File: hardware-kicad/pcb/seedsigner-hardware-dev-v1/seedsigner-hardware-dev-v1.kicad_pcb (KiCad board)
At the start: 2 copper layers, 14 x 23 mm, 17 parts, among them U1 LuckFox_Pico_MINI, U2 WAVESHARE_LCD_BUTTON_BOARD_1.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

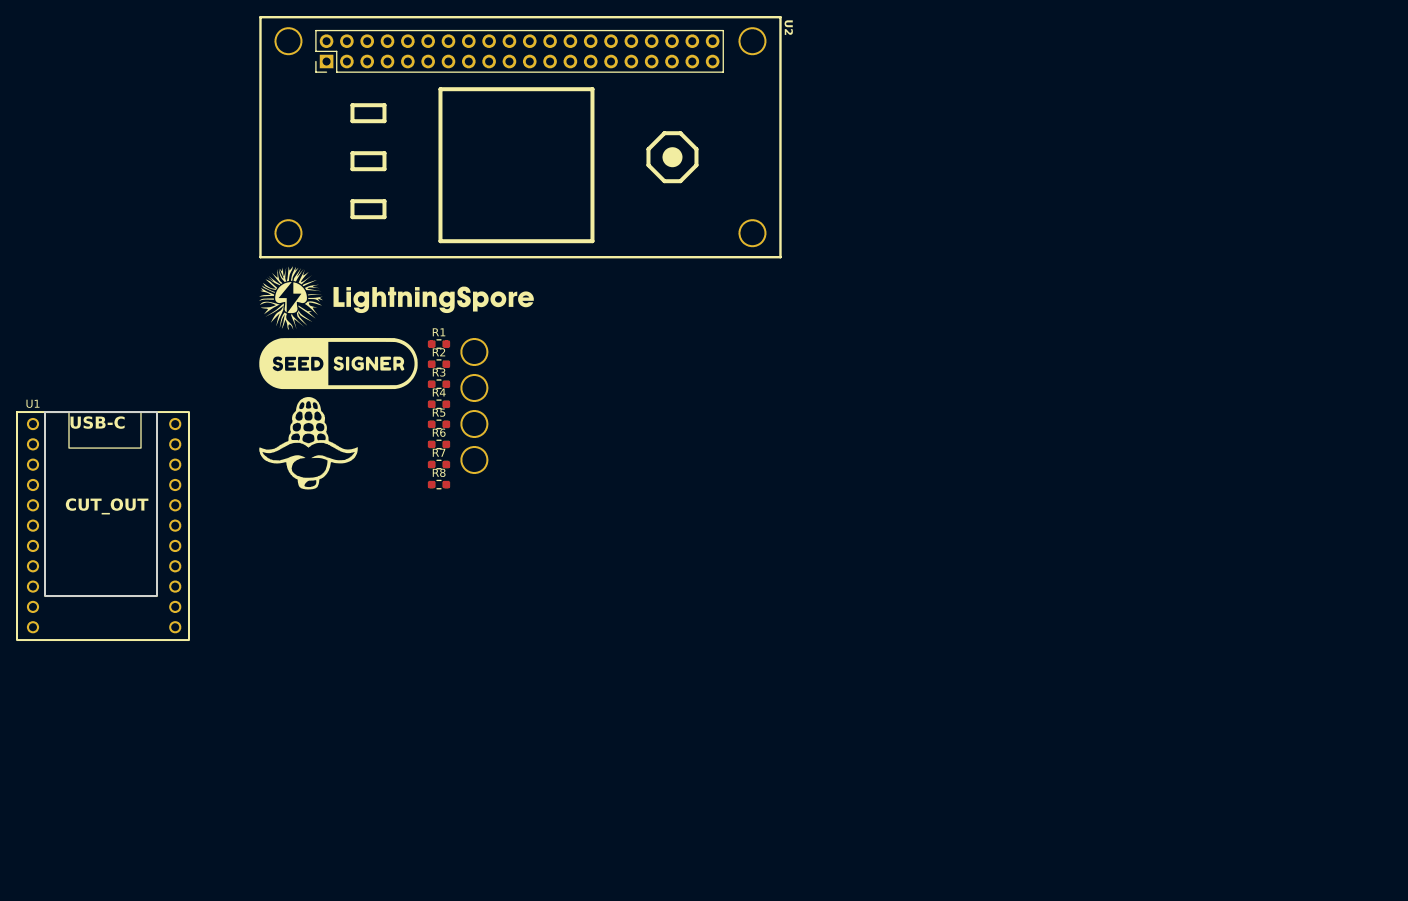
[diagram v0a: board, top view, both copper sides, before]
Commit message: seedsigner hardware dev v1 all footprints created and placed
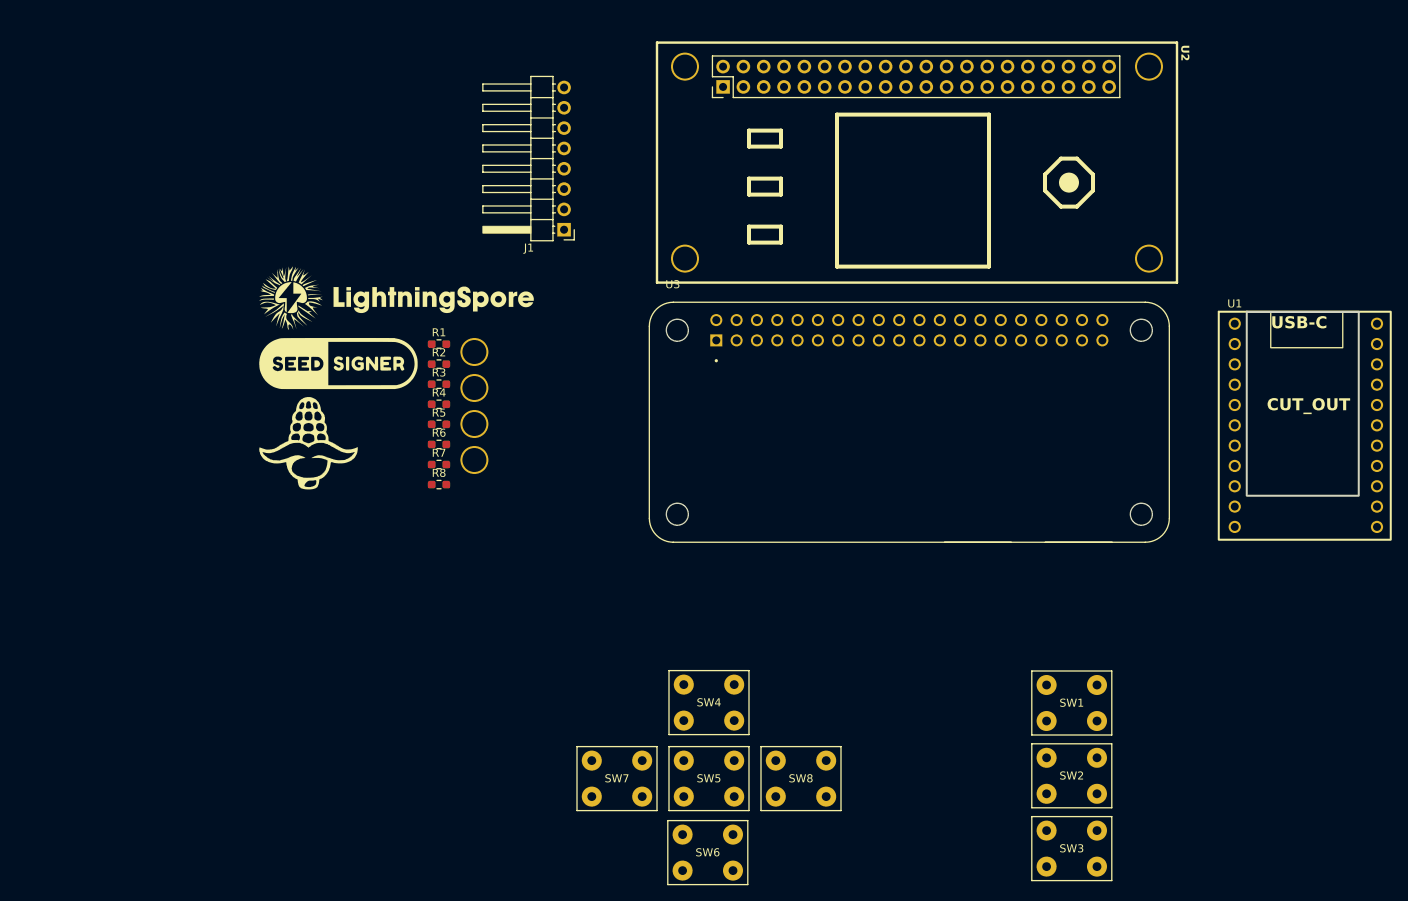
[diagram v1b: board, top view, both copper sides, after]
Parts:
- added J1: Conn_01x08_MountingPin, Connector_PinHeader_2.54mm:PinHeader_1x08_P2.54mm_Horizontal, F.Cu at (87.4, 74.9)
- added SW1: SW_Push, seedsigner-luckfox:BTN_SPST_NO_PTH, F.Cu at (150.8, 134.1)
- added SW2: SW_Push, seedsigner-luckfox:BTN_SPST_NO_PTH, F.Cu at (150.8, 143.2)
- added SW3: SW_Push, seedsigner-luckfox:BTN_SPST_NO_PTH, F.Cu at (150.8, 152.2)
- added SW4: SW_Push, seedsigner-luckfox:BTN_SPST_NO_PTH, F.Cu at (105.5, 134.0)
- added SW5: SW_Push, seedsigner-luckfox:BTN_SPST_NO_PTH, F.Cu at (105.5, 143.5)
- added SW6: SW_Push, seedsigner-luckfox:BTN_SPST_NO_PTH, F.Cu at (105.3, 152.8)
- added SW7: SW_Push, seedsigner-luckfox:BTN_SPST_NO_PTH, F.Cu at (94.0, 143.5)
- added SW8: SW_Push, seedsigner-luckfox:BTN_SPST_NO_PTH, F.Cu at (117.0, 143.5)
- added U3: RPI_ZERO, seedsigner-luckfox:RPi_Zero, F.Cu at (130.5, 99.0)
- R1, R2, R3, R4, R5, R6, R7, R8: value R -> 10K
- moved U1 150.7 mm to (171.2, 86.6)
- moved U2 49.7 mm to (131.5, 66.5)
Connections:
- R1 pad 2: /KEY3 -> /Buttons/KEY1
- R2 pad 2: /KEY2 -> /Buttons/KEY2
- R3 pad 2: /KEY1 -> /Buttons/KEY3
- R4 pad 2: /JOYSTICK_RIGHT -> /Buttons/JOYSTICK_RIGHT
- R5 pad 2: /JOYSTICK_PRESS -> /Buttons/JOYSTICK_PRESS
- R6 pad 2: /JOYSTICK_DOWN -> /Buttons/JOYSTICK_DOWN
- R7 pad 2: /JOYSTICK_UP -> /Buttons/JOYSTICK_UP
- R8 pad 2: /JOYSTICK_LEFT -> /Buttons/JOYSTICK_LEFT
- U1 pad 18: /KEY2 -> /BACKLIGHT_PWM
- U1 pad 5: /BACKLIGHT_PWM -> /KEY2

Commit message: hardware devboard changes and footprints for LCD screens
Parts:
- moved H1 113.8 mm to (3.00, 3.00)
- moved J1 90.2 mm to (11.4, 26.4)
- moved U1 90.2 mm to (95.2, 38.1)
- moved U2 90.2 mm to (55.5, 18.0)
- moved U3 90.2 mm to (54.5, 50.4)
- moved ART1 88.0 mm to (-15.7, 52.8)
- moved LOGO1 88.0 mm to (-23.3, 61.0)
- moved LOGO2 88.0 mm to (-27.1, 70.9)
- moved H3 85.5 mm to (147.0, 147.0)
- moved H4 85.0 mm to (3.00, 147.0)
- moved H2 54.5 mm to (22.0, 88.5)
- moved SW1 52.6 mm to (100.3, 119.2)
- moved SW4 52.3 mm to (55.0, 120.5)
- moved SW2 52.1 mm to (100.3, 130.2)
- moved SW5 52.1 mm to (55.0, 130.5)
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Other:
- board size 14 x 23 mm -> 150 x 150 mm

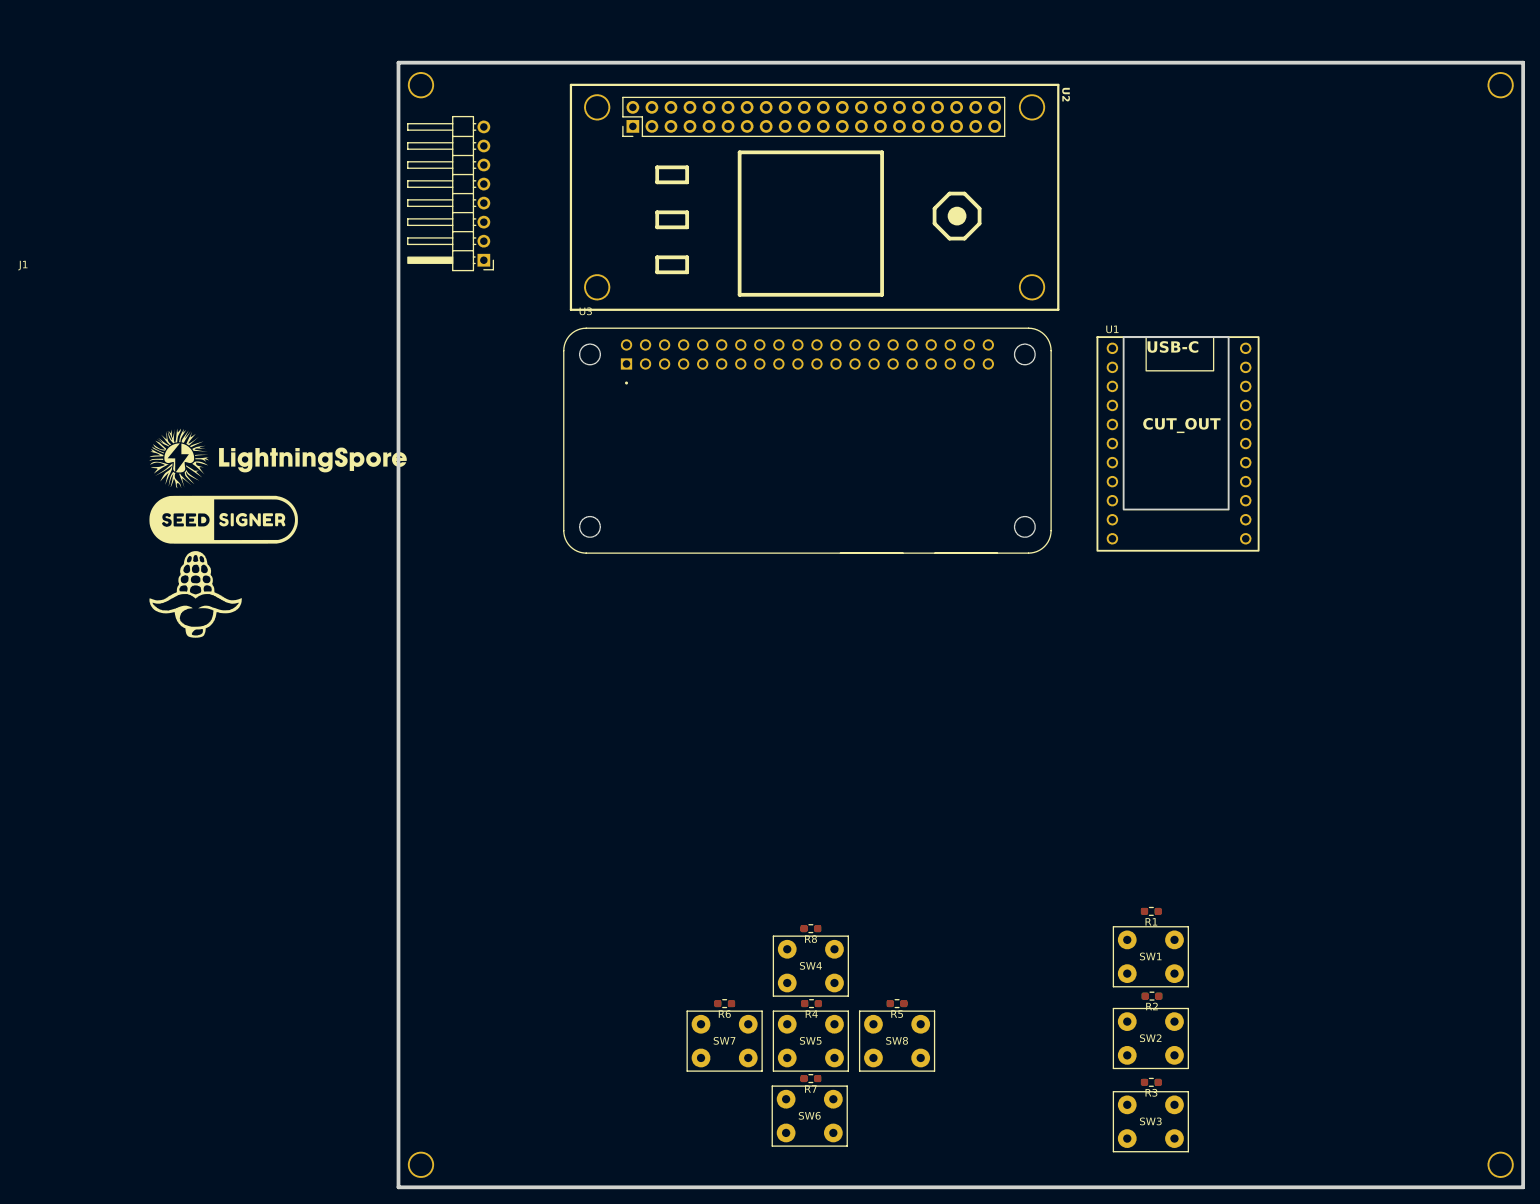
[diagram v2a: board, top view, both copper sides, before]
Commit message: use hierarchical sheets in kicad
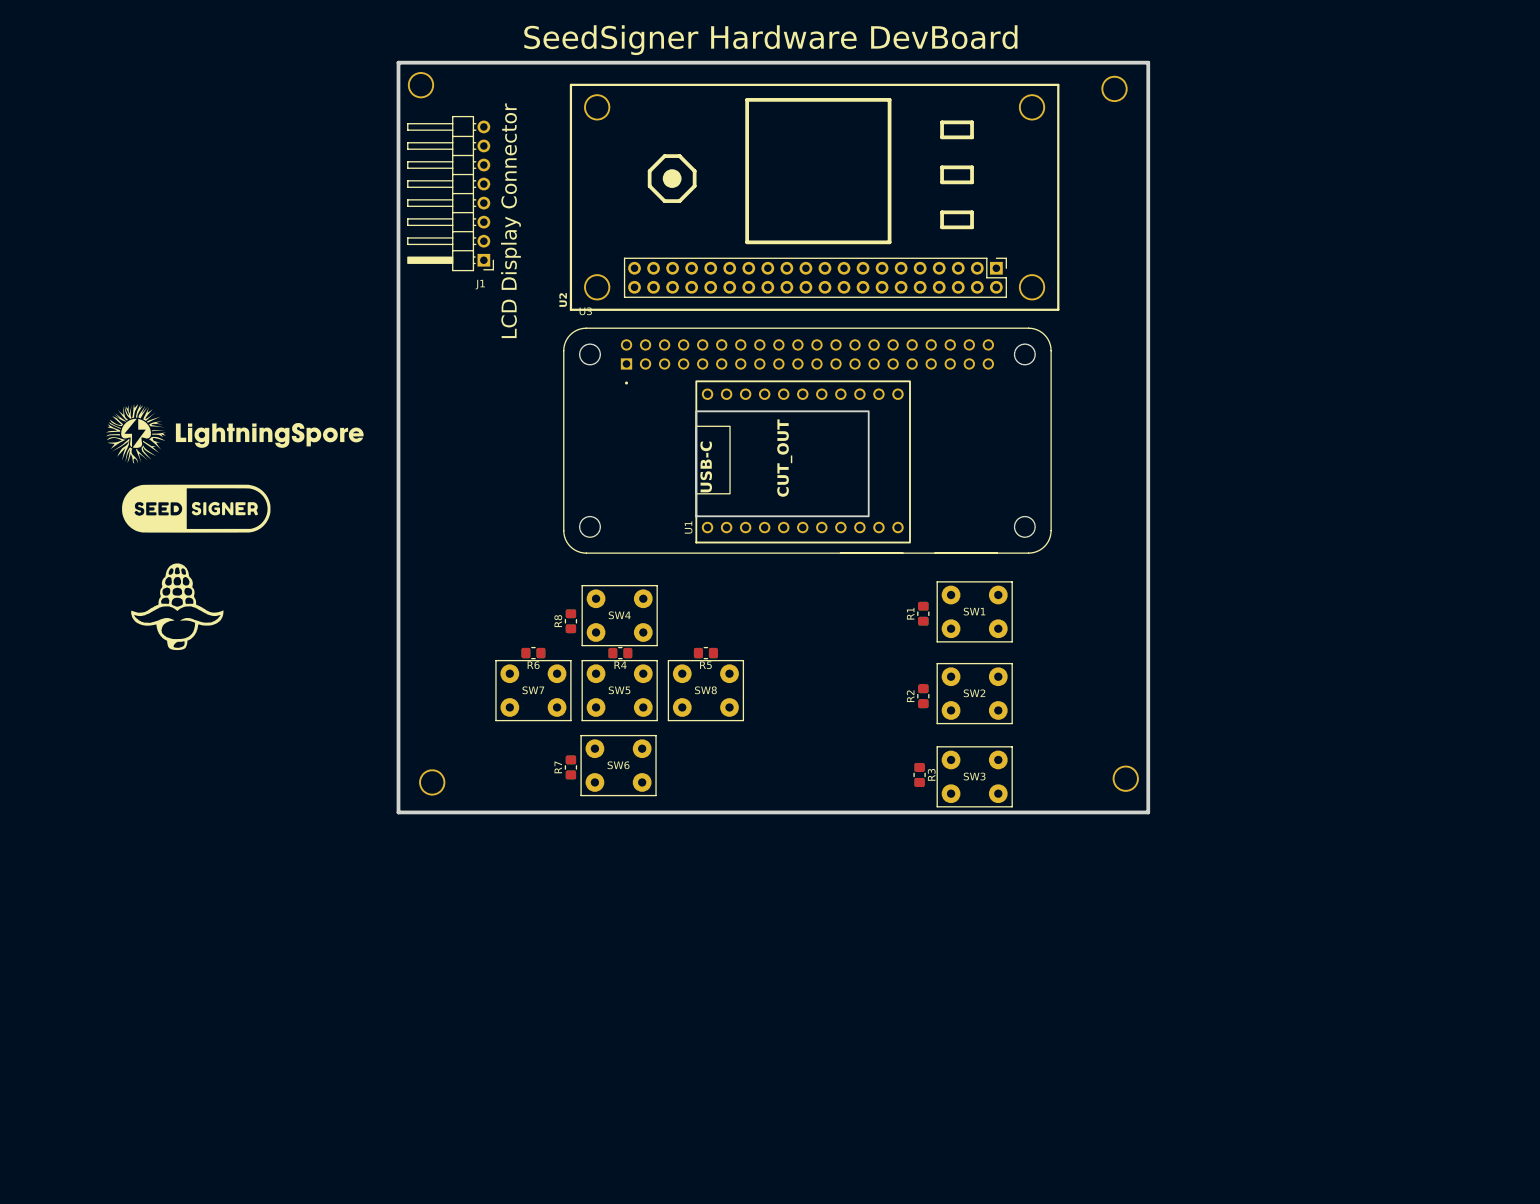
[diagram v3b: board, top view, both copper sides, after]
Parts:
- R1, R2, R3, R4, R5, R6, R7, R8: footprint Resistor_SMD:R_0603_1608Metric_Pad0.98x0.95mm_HandSolder -> Resistor_SMD:R_0805_2012Metric_Pad1.20x1.40mm_HandSolder
- moved H3 71.8 mm to (97.0, 95.5)
- moved U1 59.1 mm to (41.2, 62.0), turned to 90 degrees
- moved R4 53.3 mm to (29.6, 78.8)
- moved R5 53.3 mm to (41.0, 78.8)
- moved R6 53.3 mm to (18.0, 78.8)
- moved SW4 53.3 mm to (29.5, 73.8)
- moved SW5 53.3 mm to (29.5, 83.8)
- moved SW6 53.3 mm to (29.4, 93.8)
- moved SW7 53.3 mm to (18.0, 83.8)
- moved SW8 53.3 mm to (41.0, 83.8)
- moved R7 52.4 mm to (23.0, 94.0), turned to 90 degrees
- moved R8 52.0 mm to (23.0, 74.5), turned to 90 degrees
- moved SW1 51.7 mm to (76.8, 73.2)
- moved SW2 51.7 mm to (76.8, 84.2)
- moved SW3 51.7 mm to (76.8, 95.2)
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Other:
- board size 150 x 150 mm -> 100 x 100 mm
- board text added: "LCD Display Connector"
- board text added: "SeedSigner Hardware DevBoard"

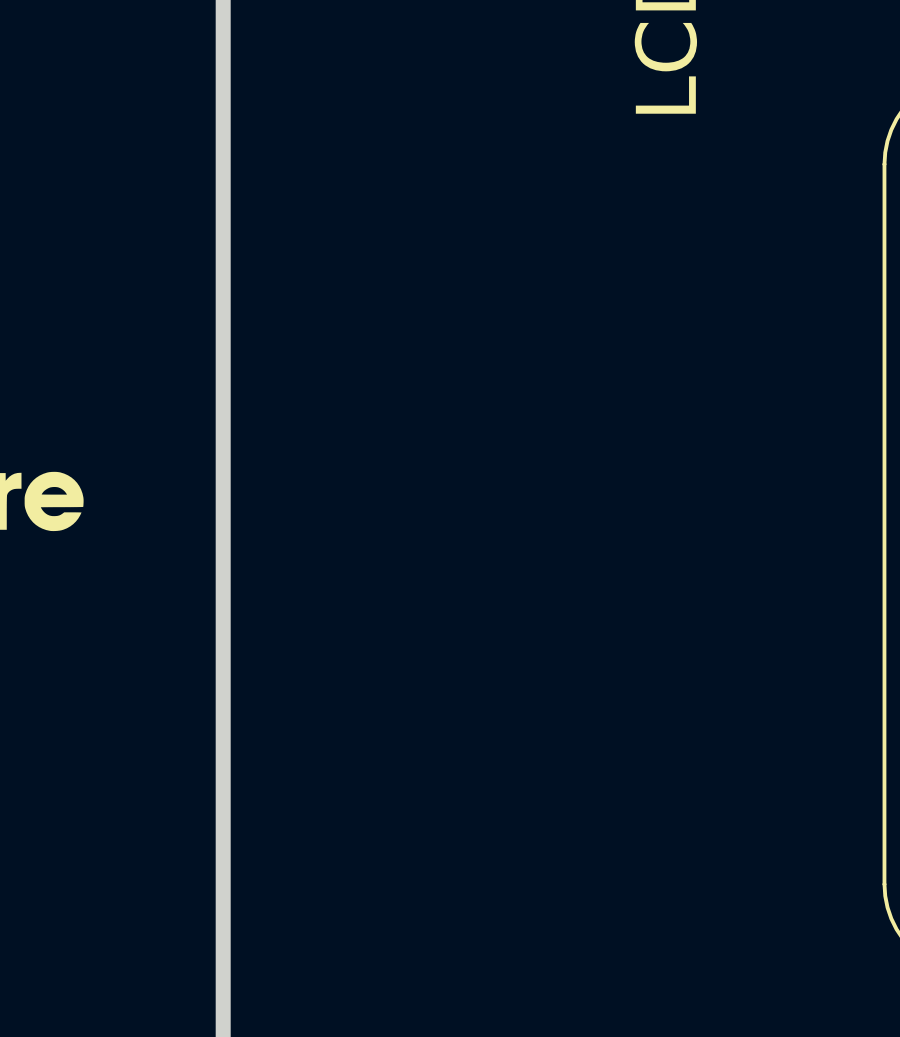
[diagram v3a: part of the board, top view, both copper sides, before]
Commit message: update library paths and modularize sch
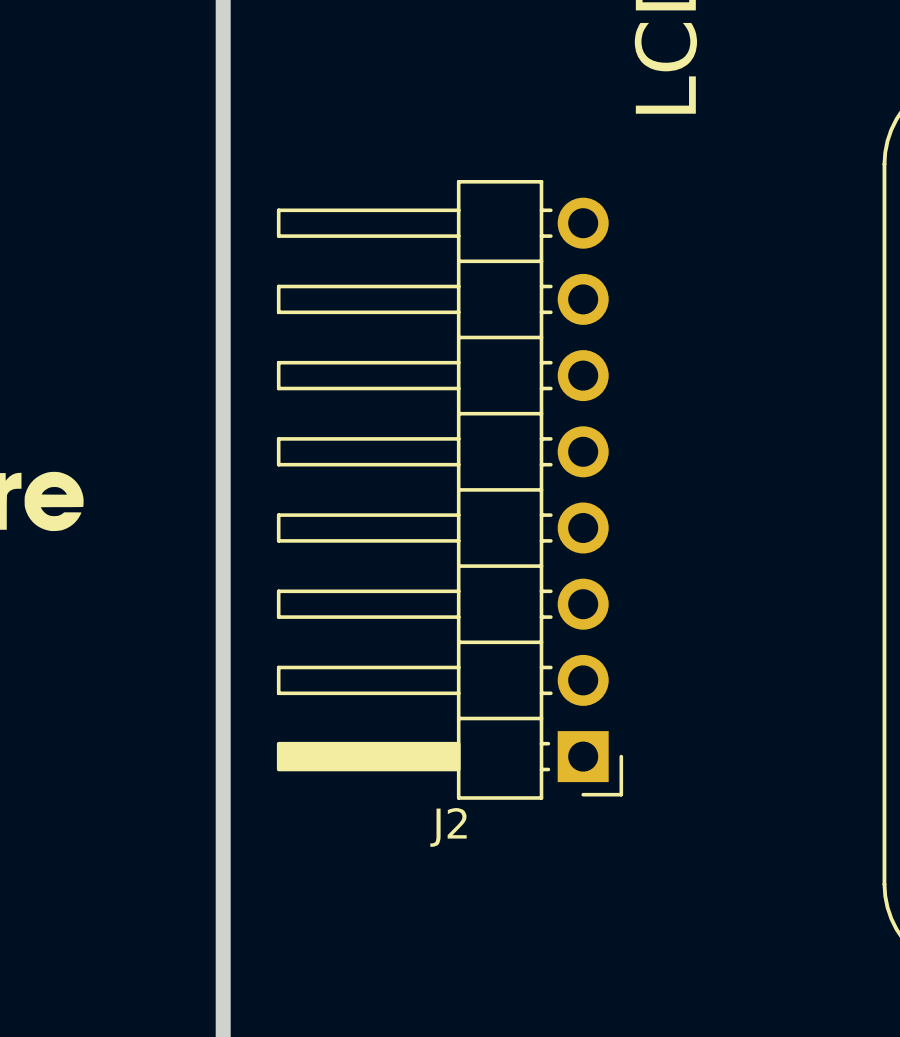
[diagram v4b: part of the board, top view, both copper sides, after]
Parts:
- added J2: Conn_01x08_MountingPin, Connector_PinHeader_2.54mm:PinHeader_1x08_P2.54mm_Horizontal, F.Cu at (12.0, 58.2)
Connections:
- net /BACKLIGHT_PWM renamed /Modules/BACKLIGHT_PWM
- net /JOYSTICK_DOWN renamed /Modules/JOYSTICK_DOWN
- net /JOYSTICK_LEFT renamed /Modules/JOYSTICK_LEFT
- net /JOYSTICK_PRESS renamed /Modules/JOYSTICK_PRESS
- net /JOYSTICK_RIGHT renamed /Modules/JOYSTICK_RIGHT
- net /JOYSTICK_UP renamed /Modules/JOYSTICK_UP
- net /KEY1 renamed /Modules/KEY1
- net /KEY2 renamed /Modules/KEY2
- net /KEY3 renamed /Modules/KEY3
- U1 pad 10: /DC -> /Modules/DC
- U1 pad 6: /SPI_CS -> /Modules/SPI_CS
- U1 pad 7: /SPI_SCLK -> /Modules/SPI_SCLK
- U1 pad 8: /SPI_MOSI -> /Modules/SPI_MOSI
- U1 pad 9: /RST -> /Modules/RST
- U2 pad 13: /RST -> /Modules/RST
- U2 pad 18: /BACKLIGHT -> /Modules/BACKLIGHT
- U2 pad 19: /SPI_MOSI -> /Modules/SPI_MOSI
- U2 pad 22: /DC -> /Modules/DC
- U2 pad 23: /SPI_SCLK -> /Modules/SPI_SCLK
- U2 pad 24: /SPI_CS -> /Modules/SPI_CS
- U3 pad 13: /RST -> /Modules/RST
- U3 pad 18: /BACKLIGHT -> /Modules/BACKLIGHT
- U3 pad 19: /SPI_MOSI -> /Modules/SPI_MOSI
- U3 pad 22: /DC -> /Modules/DC
- U3 pad 23: /SPI_SCLK -> /Modules/SPI_SCLK
- U3 pad 24: /SPI_CS -> /Modules/SPI_CS
